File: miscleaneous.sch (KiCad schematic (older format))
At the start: 8 parts

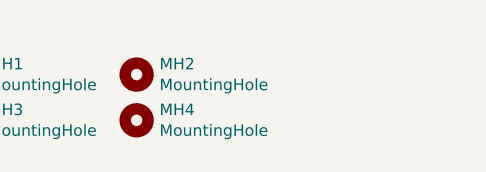
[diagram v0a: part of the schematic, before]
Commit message: Fixes PCB, reset esp32
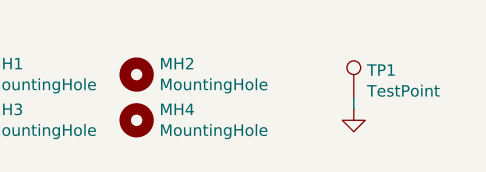
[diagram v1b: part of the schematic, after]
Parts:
- added TP1: TestPoint, symbol Connector:TestPoint
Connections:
- new net GND: TP1.1
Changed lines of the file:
@@
 	1    0    0    -1
 $EndComp
+$Comp
+L Connector:TestPoint TP1
+U 1 1 61744F6A
+P 7450 4200
+F 0 "TP1" H 7508 4318 50  0000 L CNN
+F 1 "TestPoint" H 7508 4227 50  0000 L CNN
+F 2 "" H 7650 4200 50  0001 C CNN
+F 3 "~" H 7650 4200 50  0001 C CNN
+	1    7450 4200
+	1    0    0    -1
+$EndComp
+$Comp
+L 00_lib_sch:GND #PWR?
+U 1 1 61747087
+P 7450 4250
+F 0 "#PWR?" H 7450 4000 50  0001 C CNN
+F 1 "GND" H 7455 4077 50  0001 C CNN
+F 2 "" H 7450 4250 50  0001 C CNN
+F 3 "" H 7450 4250 50  0001 C CNN
+	1    7450 4250
+	1    0    0    -1
+$EndComp
+Wire Wire Line
+	7450 4250 7450 4200
 $EndSCHEMATC

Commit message: Fix por revision grupal
    *Fix de memoria de i2c, mal sda y scl
    *Fix inpunts sda y scl
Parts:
- TP1: footprint (none) -> 00_lib_fp:TestPoint_Plated_Hole_D2.0mm
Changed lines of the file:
@@
 F 0 "TP1" H 7508 4318 50  0000 L CNN
 F 1 "TestPoint" H 7508 4227 50  0000 L CNN
-F 2 "" H 7650 4200 50  0001 C CNN
+F 2 "00_lib_fp:TestPoint_Plated_Hole_D2.0mm" H 7650 4200 50  0001 C CNN
 F 3 "~" H 7650 4200 50  0001 C CNN
 	1    7450 4200
